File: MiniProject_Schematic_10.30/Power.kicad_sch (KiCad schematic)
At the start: 14 parts, among them J1 10118194-0001LF, U10 LM66100DCK, U11 AP2112K-3.3TRG1, U2 LM66100DCK

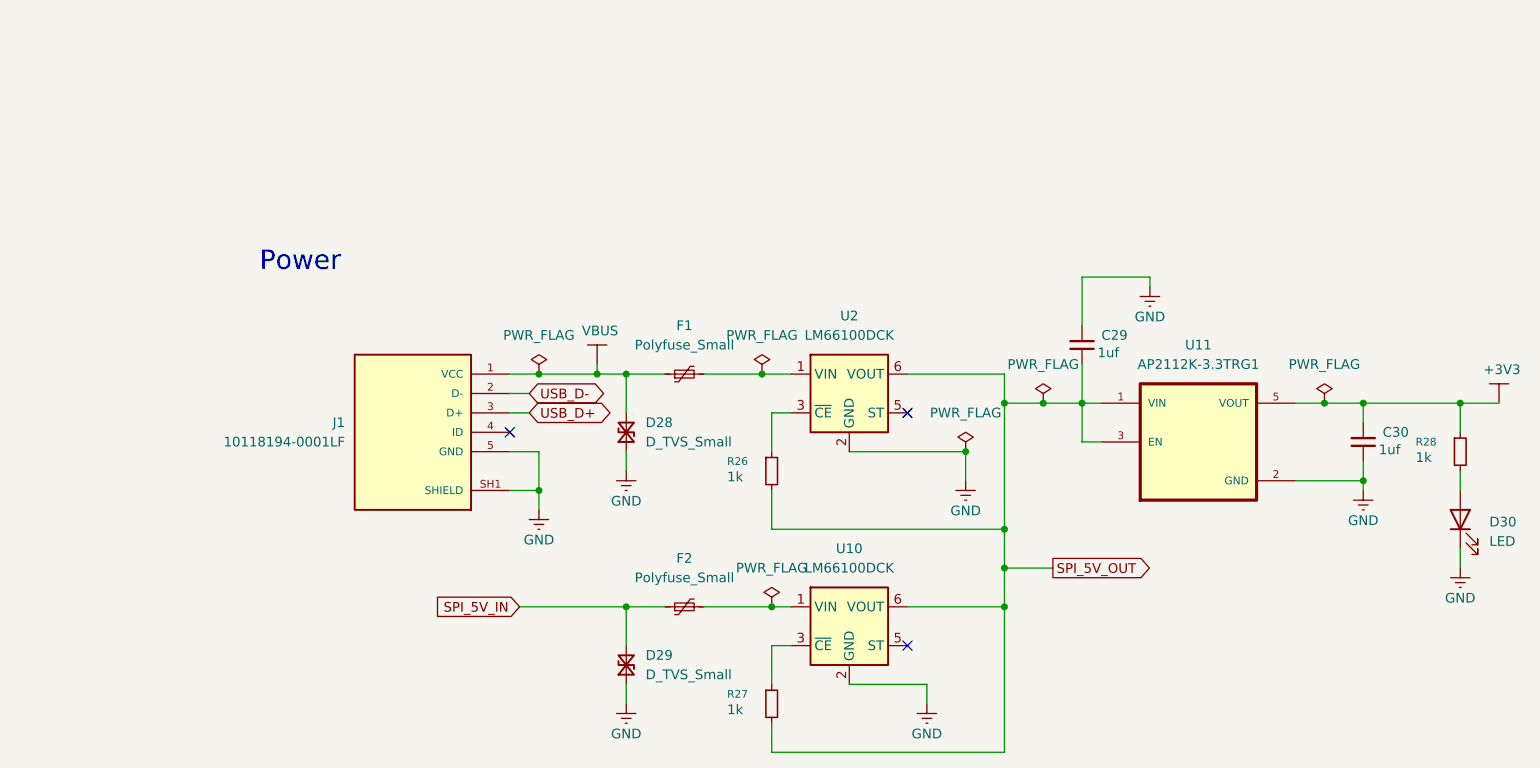
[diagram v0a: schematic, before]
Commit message: Correct the schematic diagram
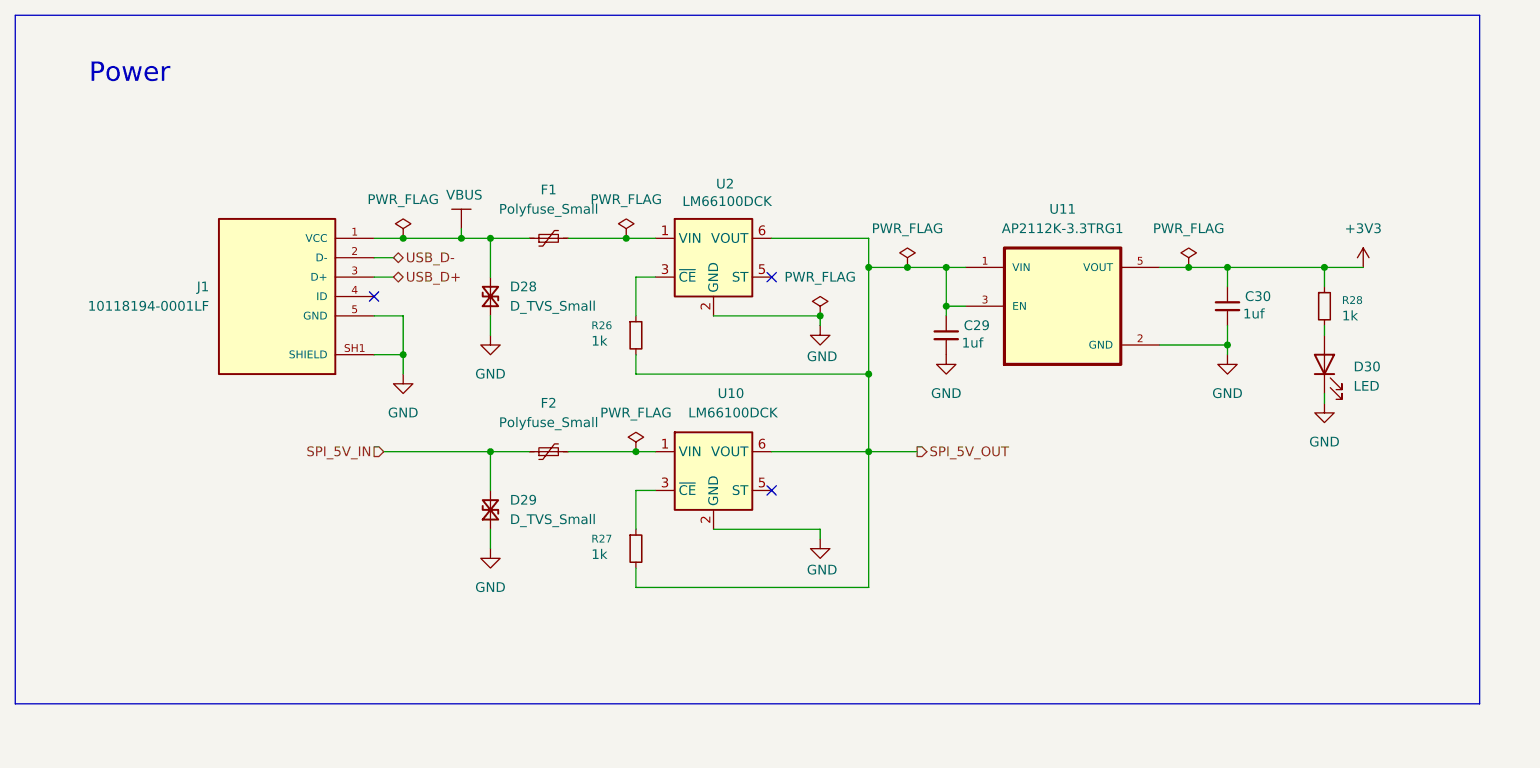
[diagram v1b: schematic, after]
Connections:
- net GND: now also C29.2; no longer C29.1
- net SPI_5V_OUT: now also C29.1; no longer C29.2
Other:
- moved on the sheet: C30, D28, D29, D30, F1, F2, J1, R26, R27, R28, U10, U11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
